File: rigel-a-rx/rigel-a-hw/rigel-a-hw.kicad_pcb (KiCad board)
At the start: 4 copper layers, 35 x 20 mm, 37 parts, among them IC1 BALFHB-WL-02D3, J1 Conn_01x03_Pin, J3 Conn_01x03_Pin, U1 STM32WLE5C8Ux, U2 XC6206P332MR, U3 CH340X, U4 TYPE-C_16PIN_2MD(073), U5 X1G004131004200, U6 KH-SMA-K513-G

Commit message: add finishing touches to pcb
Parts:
- added G***: LOGO, jlc:orion-logo, F.Cu at (111.6, 114.7)
- added G***: LOGO, jlc:orion-logo, B.Cu at (111.1, 114.7)
- added H1: MountingHole, MountingHole:MountingHole_2.2mm_M2, F.Cu at (132.4, 117.5)
- added H2: MountingHole, MountingHole:MountingHole_2.2mm_M2, F.Cu at (102.5, 117.5)
- moved J1 1.16 mm to (127.3, 118.3)
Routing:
- net GND: vias 217 -> 212
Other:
- board text added: "AD ASTRA"
- board text added: "GROUND STATION"
- board text added: "RIGEL A"

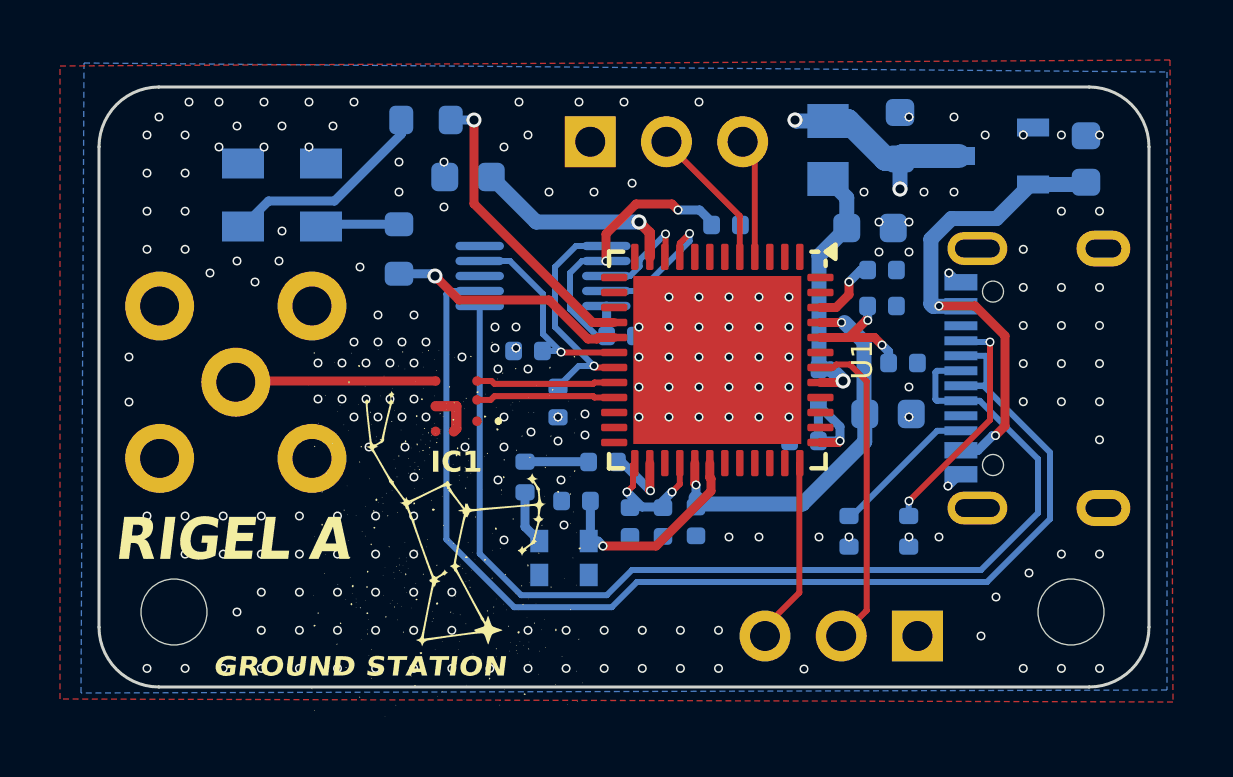
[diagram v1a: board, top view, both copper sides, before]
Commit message: basic RX test working
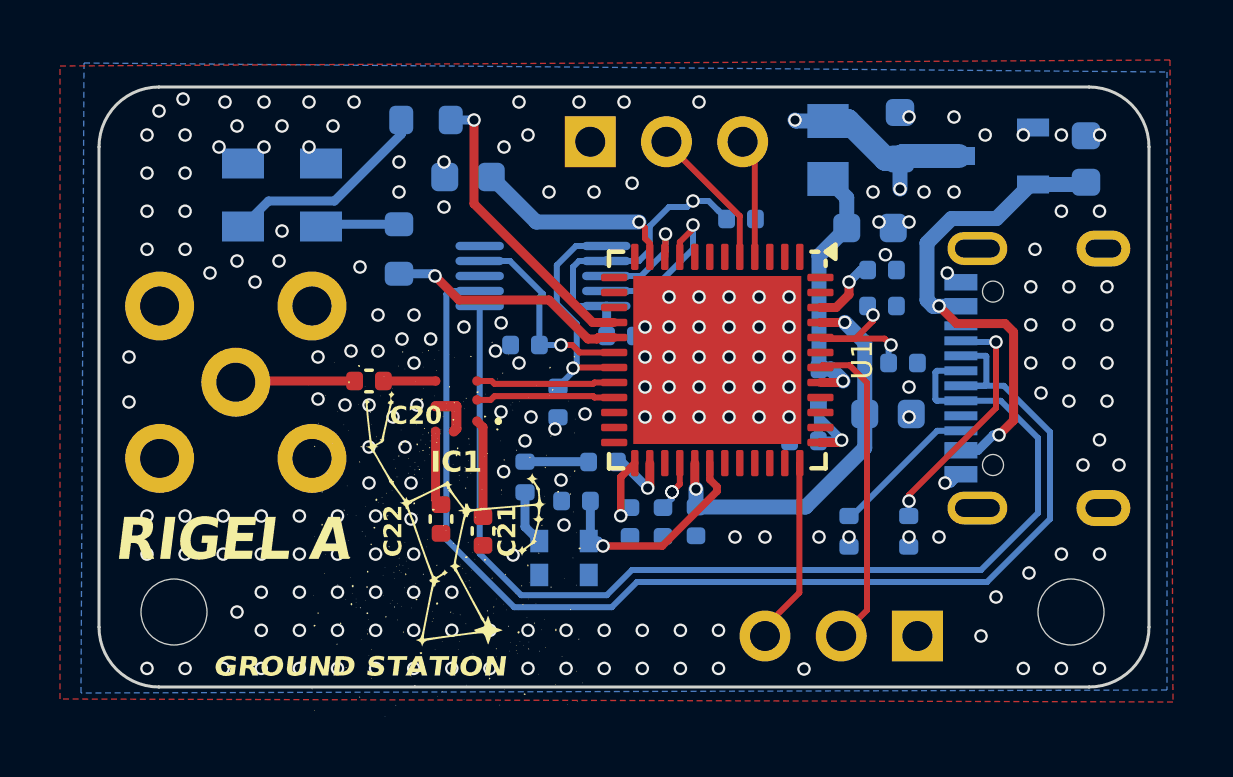
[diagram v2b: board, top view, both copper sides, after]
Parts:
- added C20: 68pF, Capacitor_SMD:C_0402_1005Metric, F.Cu at (109.0, 109.8)
- added C21: 68pF, Capacitor_SMD:C_0402_1005Metric, F.Cu at (112.8, 114.8)
- added C22: 68pF, Capacitor_SMD:C_0402_1005Metric, F.Cu at (111.4, 114.4)
- moved C12 0.54 mm to (121.4, 104.4)
- moved C13 0.22 mm to (114.2, 108.6)
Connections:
- IC1 pad A1: unconnected-(IC1-RFO_IN-PadA1) -> Net-(IC1-RFO_IN)
- IC1 pad C1: unconnected-(IC1-RFO_OUT-PadC1) -> Net-(IC1-RFO_OUT)
- U6 pad 5: Net-(IC1-RFI_IN) -> Net-(U6-IN)
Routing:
- net Net-(IC1-RFI_IN): track 6.62 -> 1.74 mm
- net Net-(U6-IN): track 0.00 -> 3.98 mm
- net Net-(IC1-RFO_IN): track 0.00 -> 3.26 mm
- net Net-(IC1-RFO_OUT): track 0.00 -> 2.51 mm
- net +3.3V: track 38.9 -> 40.5 mm
- net /USART2_TX: track 4.63 -> 5.51 mm
- net +5V: track 17.1 -> 17.7 mm
- net GND: track 2.56 -> 2.81 mm, vias 212 -> 201
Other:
- board text added: "JLCJLCJLCJLC"
